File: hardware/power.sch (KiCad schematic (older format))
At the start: 31 parts

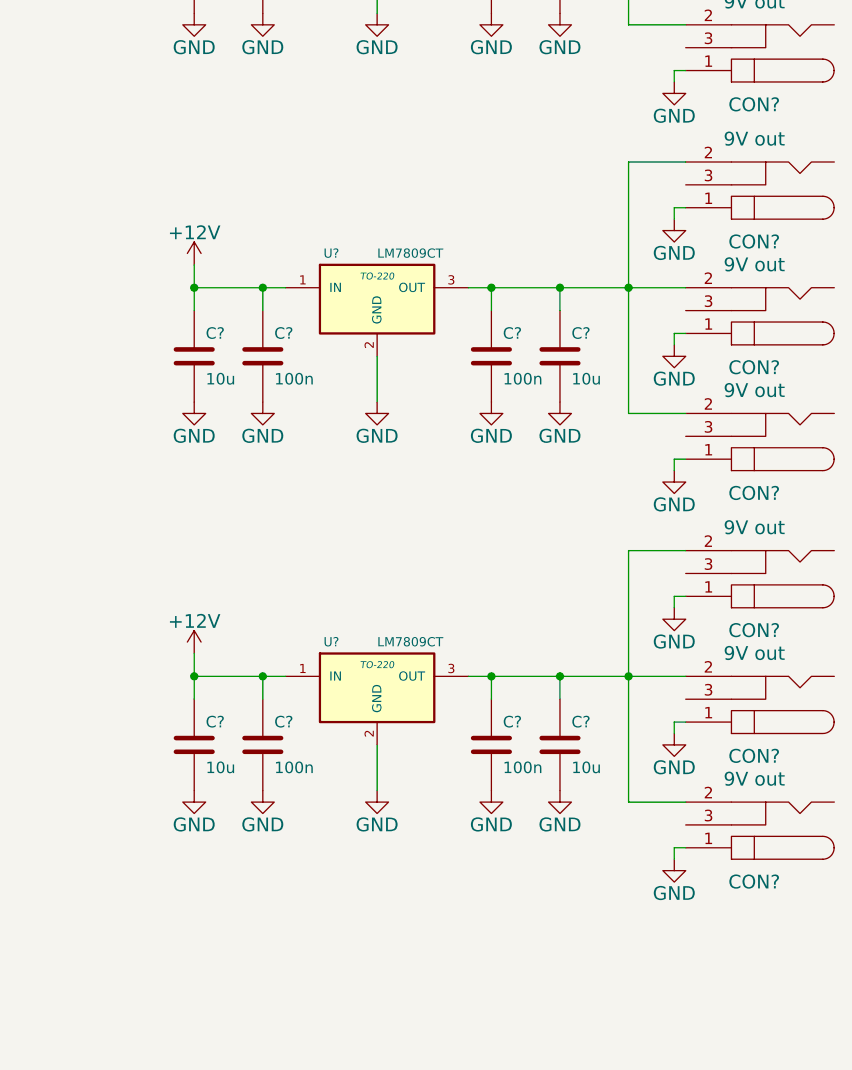
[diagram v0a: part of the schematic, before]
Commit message: Adapt number of 9V outputs
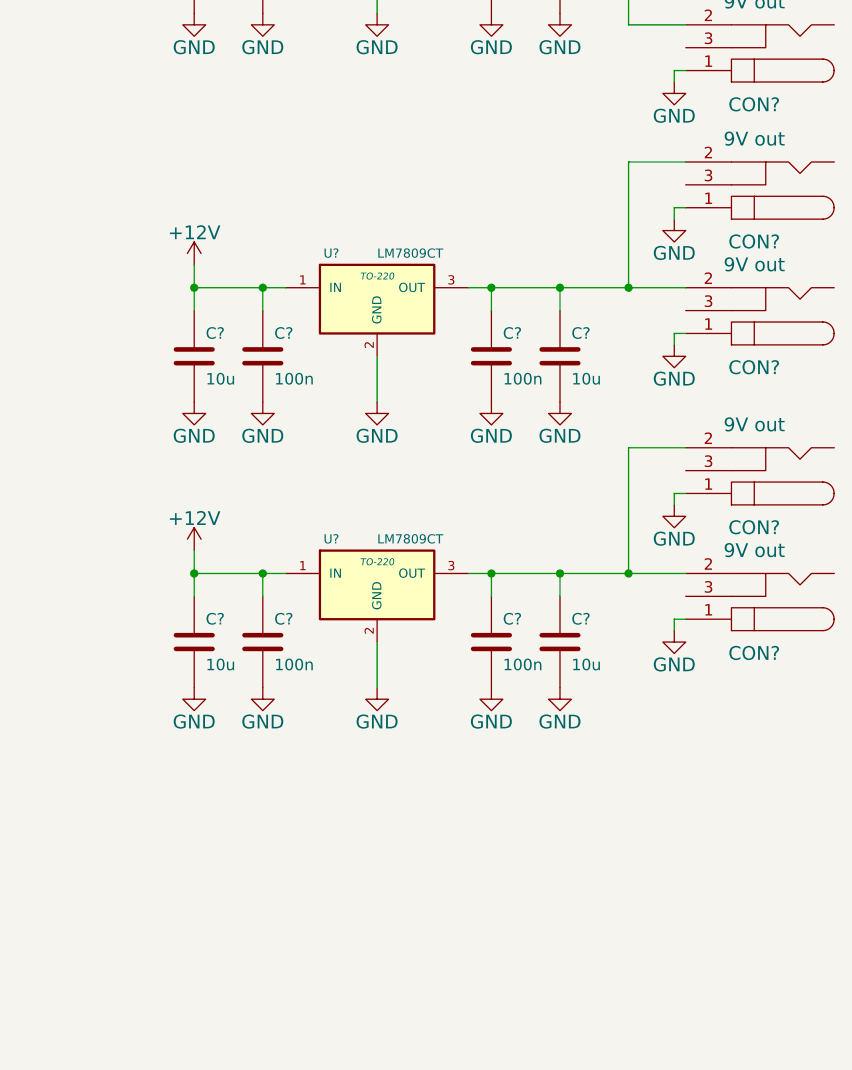
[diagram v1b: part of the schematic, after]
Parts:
- removed CON? (x2): 9V out, symbol BARREL_JACK
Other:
- moved on the sheet: C?, CON?, U?

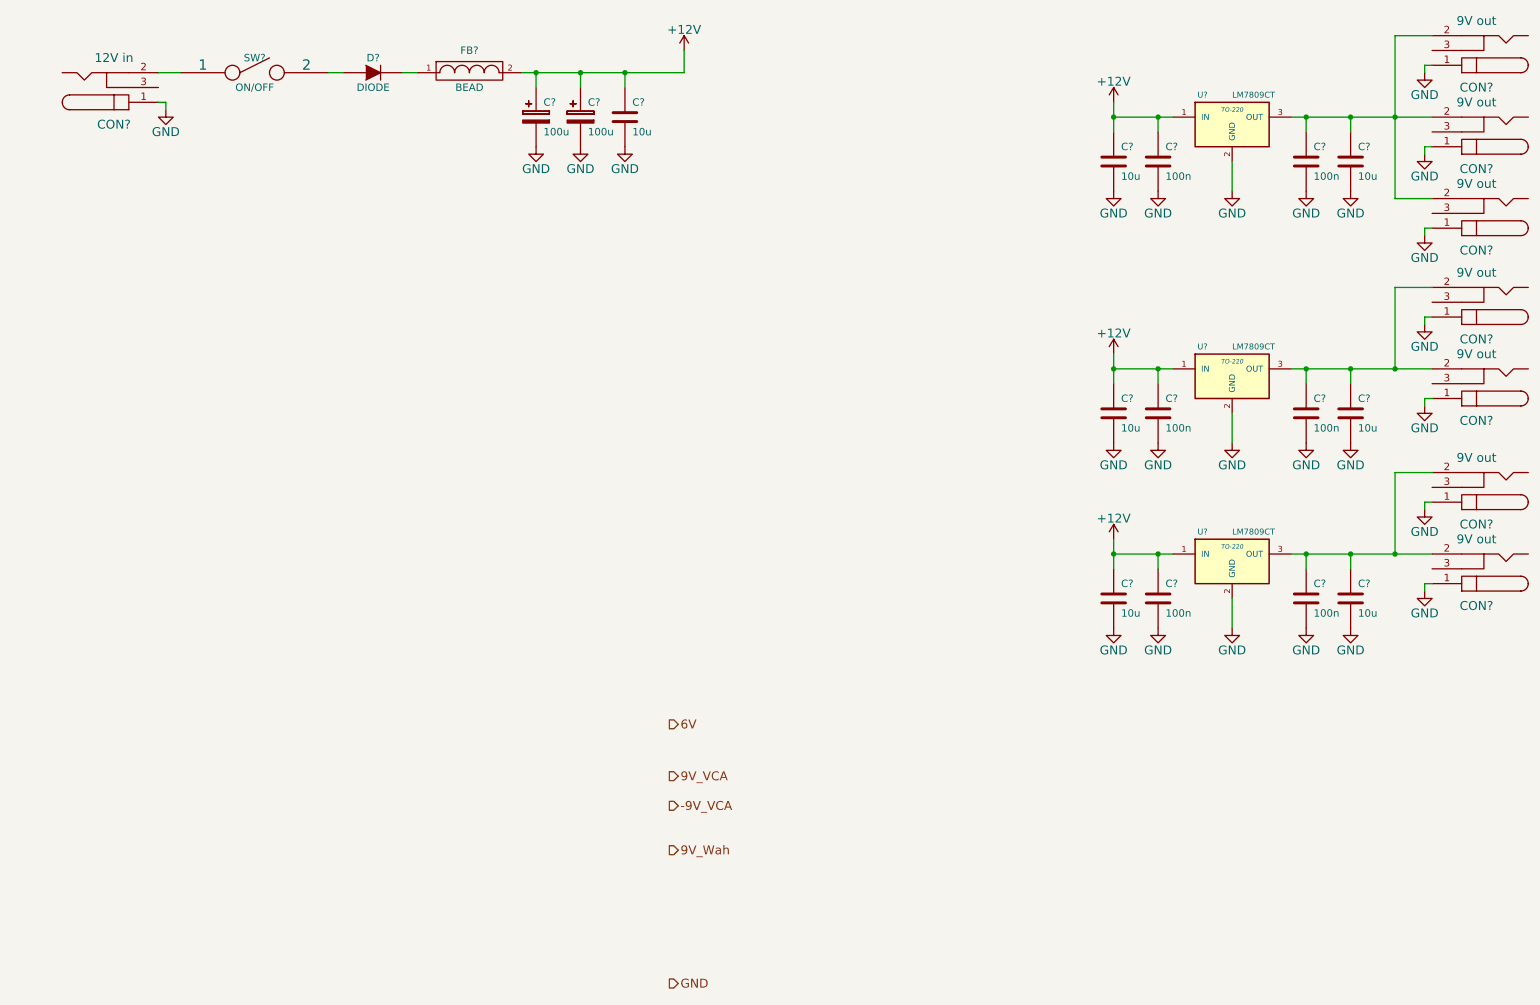
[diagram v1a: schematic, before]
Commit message: Draw VCA power supply
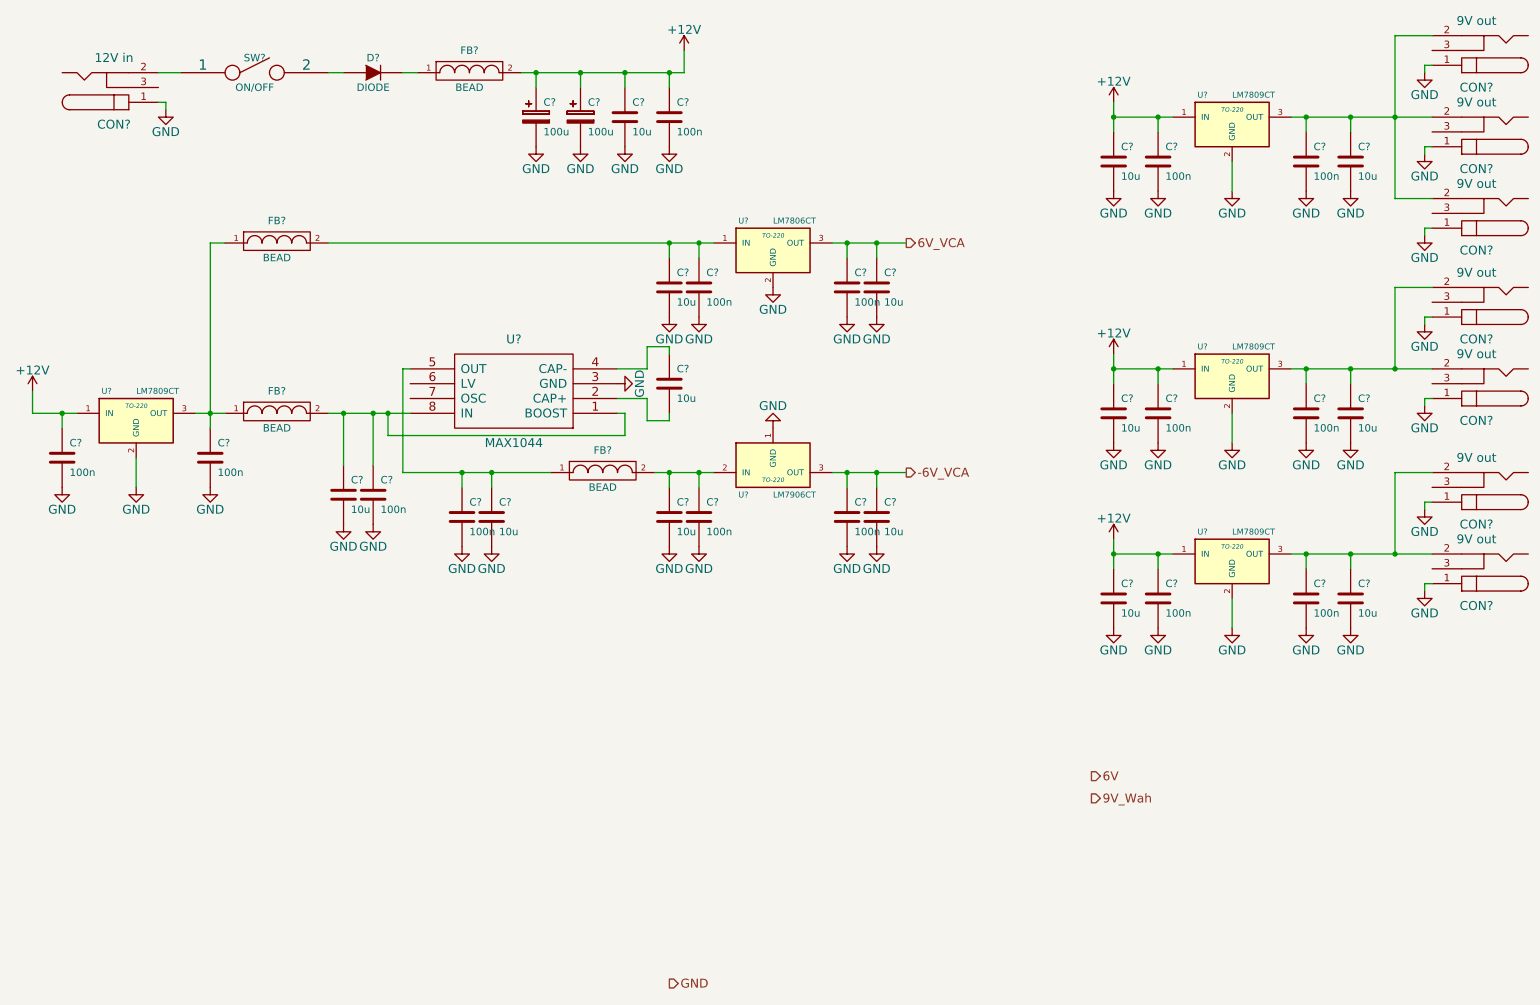
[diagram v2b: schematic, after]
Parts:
- added C? (x9): 100n, symbol C
- added C? (x7): 10u, symbol C
- added FB? (x3): BEAD, symbol FILTER
- added U?: MAX1044, symbol MAX1044
- added U?: LM7809CT, TO-220, symbol LM7809CT
- added U?: LM7906CT, TO-220, symbol LM7906CT
- added U?: LM7806CT, TO-220, symbol LM7806CT
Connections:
- net +12V: now also C?.1, C?.1, U?.1 (IN)
- net GND: now also C?.2, C?.2, C?.2, C?.2, C?.2, C?.2, C?.2, C?.2, C?.2, C?.2, C?.2, C?.2, C?.2, C?.2, C?.2, U?.1 (GND), U?.2 (GND), U?.2 (GND), U?.3 (GND)
- new net: C?.1, C?.1, FB?.2, U?.1 (BOOST), U?.8 (IN)
- new net: C?.2, U?.2 (CAP+)
- new net: C?.1, U?.4 (CAP-)
- new net: C?.1, C?.1, FB?.1, U?.5 (OUT)
- new net: C?.1, FB?.1, FB?.1, U?.3 (OUT)
- new net: C?.1, C?.1, FB?.2, U?.2 (IN)
- new net: C?.1, C?.1, FB?.2, U?.1 (IN)
- new net -6V_VCA: C?.1, C?.1, U?.3 (OUT)
- new net 6V_VCA: C?.1, C?.1, U?.3 (OUT)

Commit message: Select VCA LDOs
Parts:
- U?: value LM7906CT -> MC79L06F; footprint TO-220 -> SOT-89
- U?: value LM7806CT -> MC78L06F; footprint TO-220 -> SOT-89
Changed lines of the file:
@@
 P 5600 3750
 F 0 "U?" H 5400 3550 40  0000 C CNN
-F 1 "LM7906CT" H 5600 3550 40  0000 L CNN
-F 2 "TO-220" H 5600 3650 30  0000 C CIN
+F 1 "MC79L06F" H 5600 3550 40  0000 L CNN
+F 2 "SOT-89" H 5600 3650 30  0000 C CIN
 F 3 "" H 5600 3750 60  0000 C CNN
 	1    5600 3750
@@
 P 5600 2300
 F 0 "U?" H 5400 2500 40  0000 C CNN
-F 1 "LM7806CT" H 5600 2500 40  0000 L CNN
-F 2 "TO-220" H 5600 2400 30  0000 C CIN
+F 1 "MC78L06F" H 5600 2500 40  0000 L CNN
+F 2 "SOT-89" H 5600 2400 30  0000 C CIN
 F 3 "" H 5600 2300 60  0000 C CNN
 	1    5600 2300

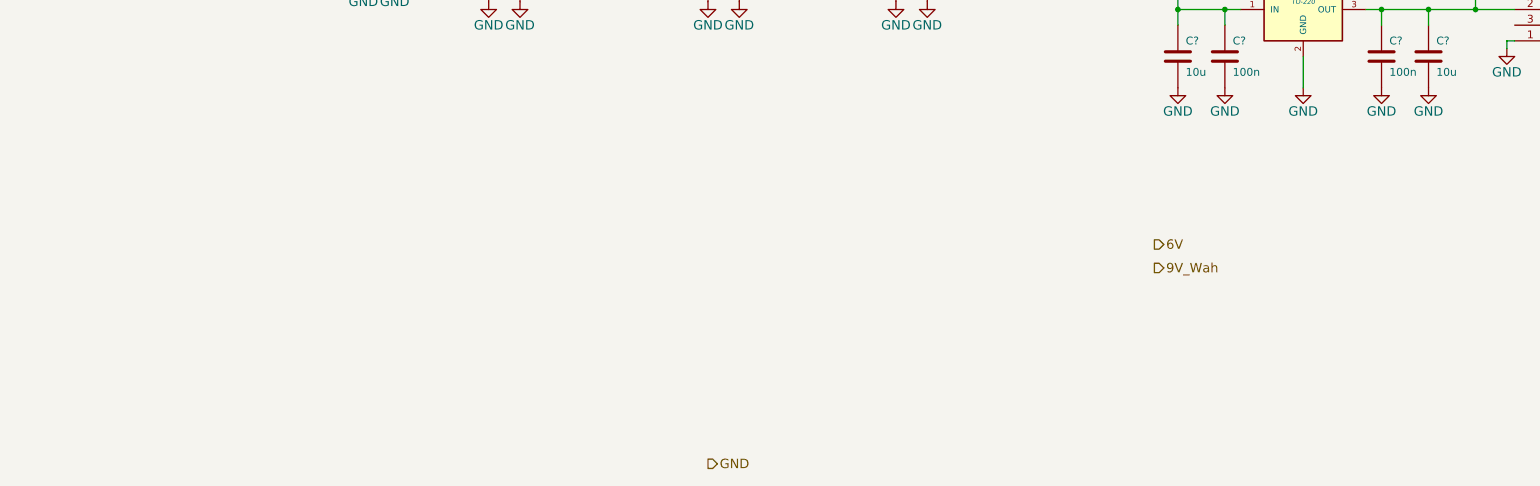
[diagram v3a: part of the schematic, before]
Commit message: Stub wah subcircuit
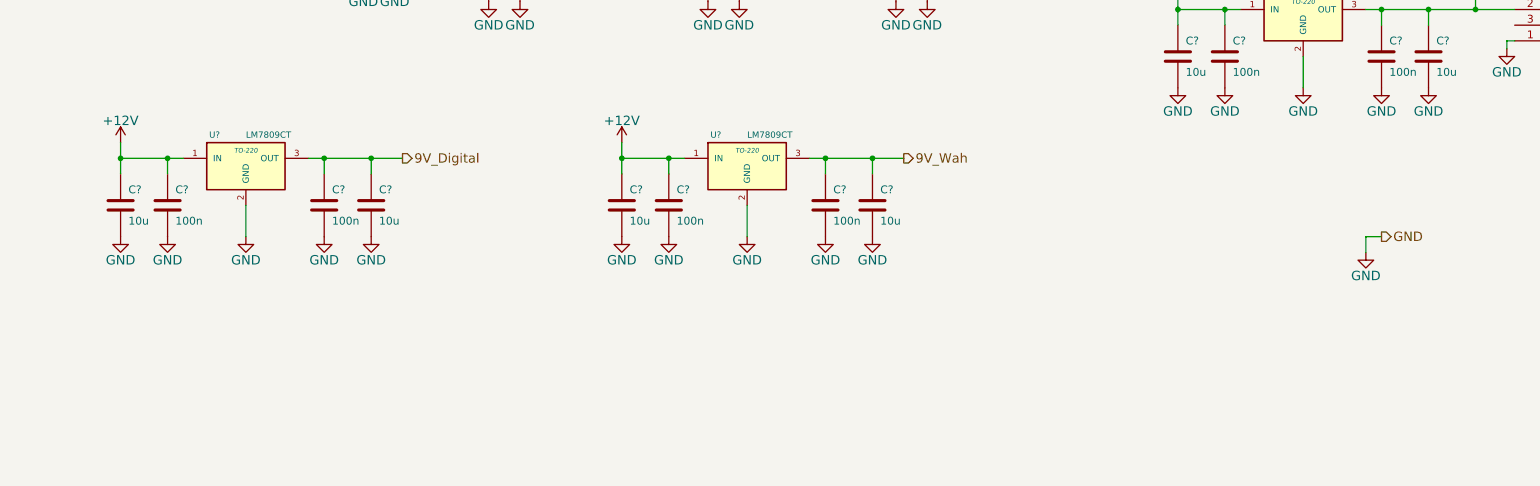
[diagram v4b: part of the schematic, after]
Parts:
- added C? (x4): 100n, symbol C
- added C? (x4): 10u, symbol C
- added U? (x2): LM7809CT, TO-220, symbol LM7809CT
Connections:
- net +12V: now also C?.1, C?.1, C?.1, C?.1, U?.1 (IN), U?.1 (IN)
- net 9V_Wah: now also C?.1, C?.1, U?.3 (OUT)
- net GND: now also C?.2, C?.2, C?.2, C?.2, C?.2, C?.2, C?.2, C?.2, U?.2 (GND), U?.2 (GND)
- new net 9V_Digital: C?.1, C?.1, U?.3 (OUT)
